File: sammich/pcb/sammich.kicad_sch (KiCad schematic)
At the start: 38 parts, among them J1 Conn_01x02, J2 Conn_02x05_Odd_Even, J3 Conn_01x04, U1 STM32F103RBTx, U2 LD3985M33R_SOT23, U3 MAX485E, Y1 Crystal

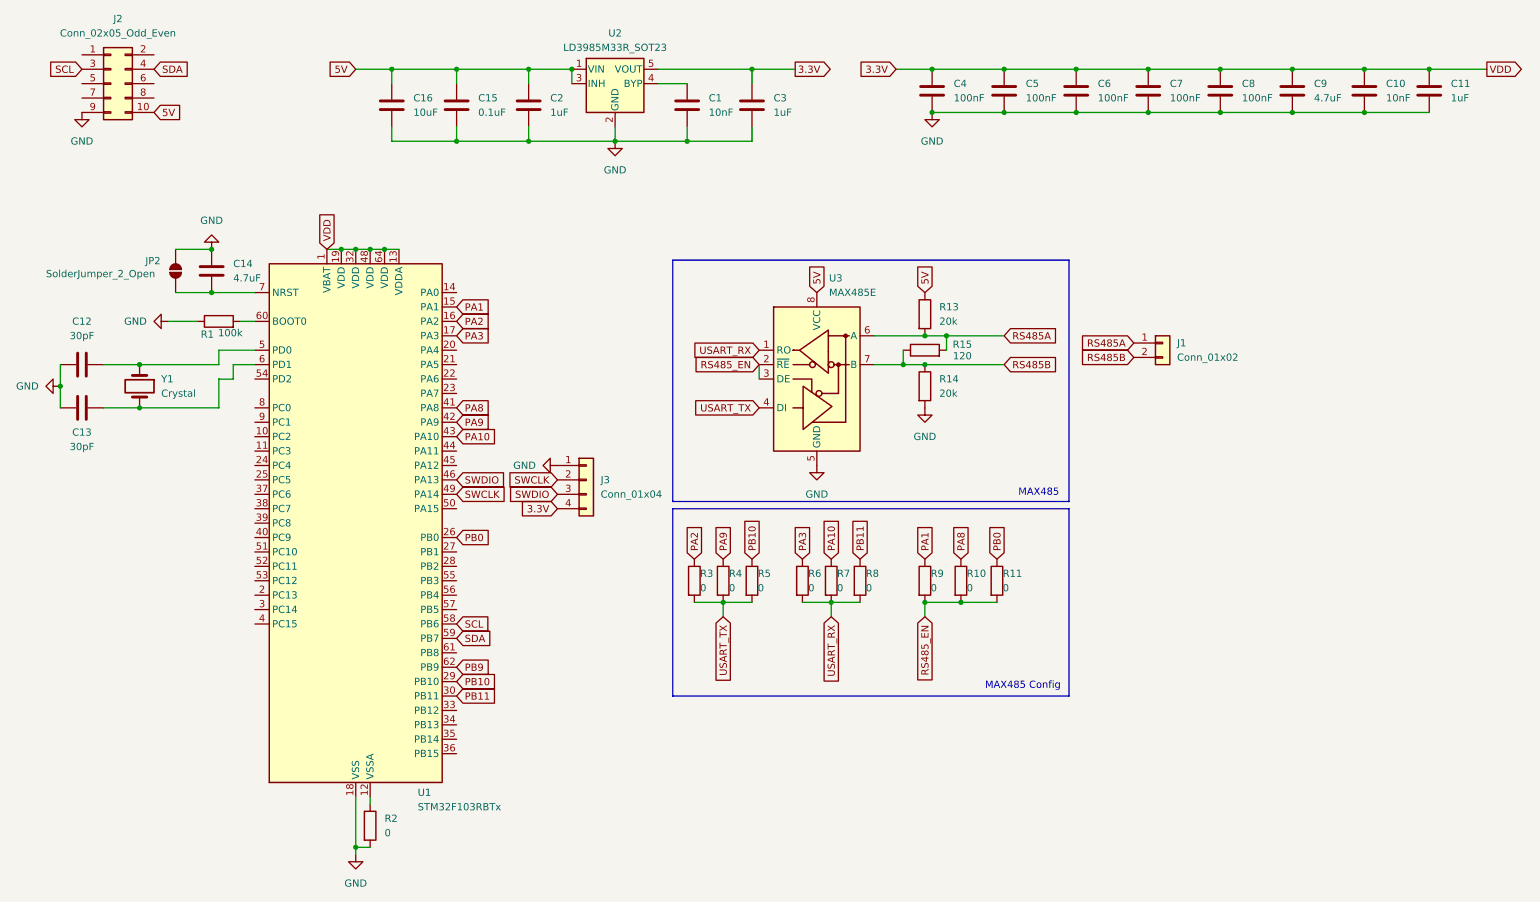
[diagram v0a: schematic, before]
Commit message: Updated PCB to use I2C
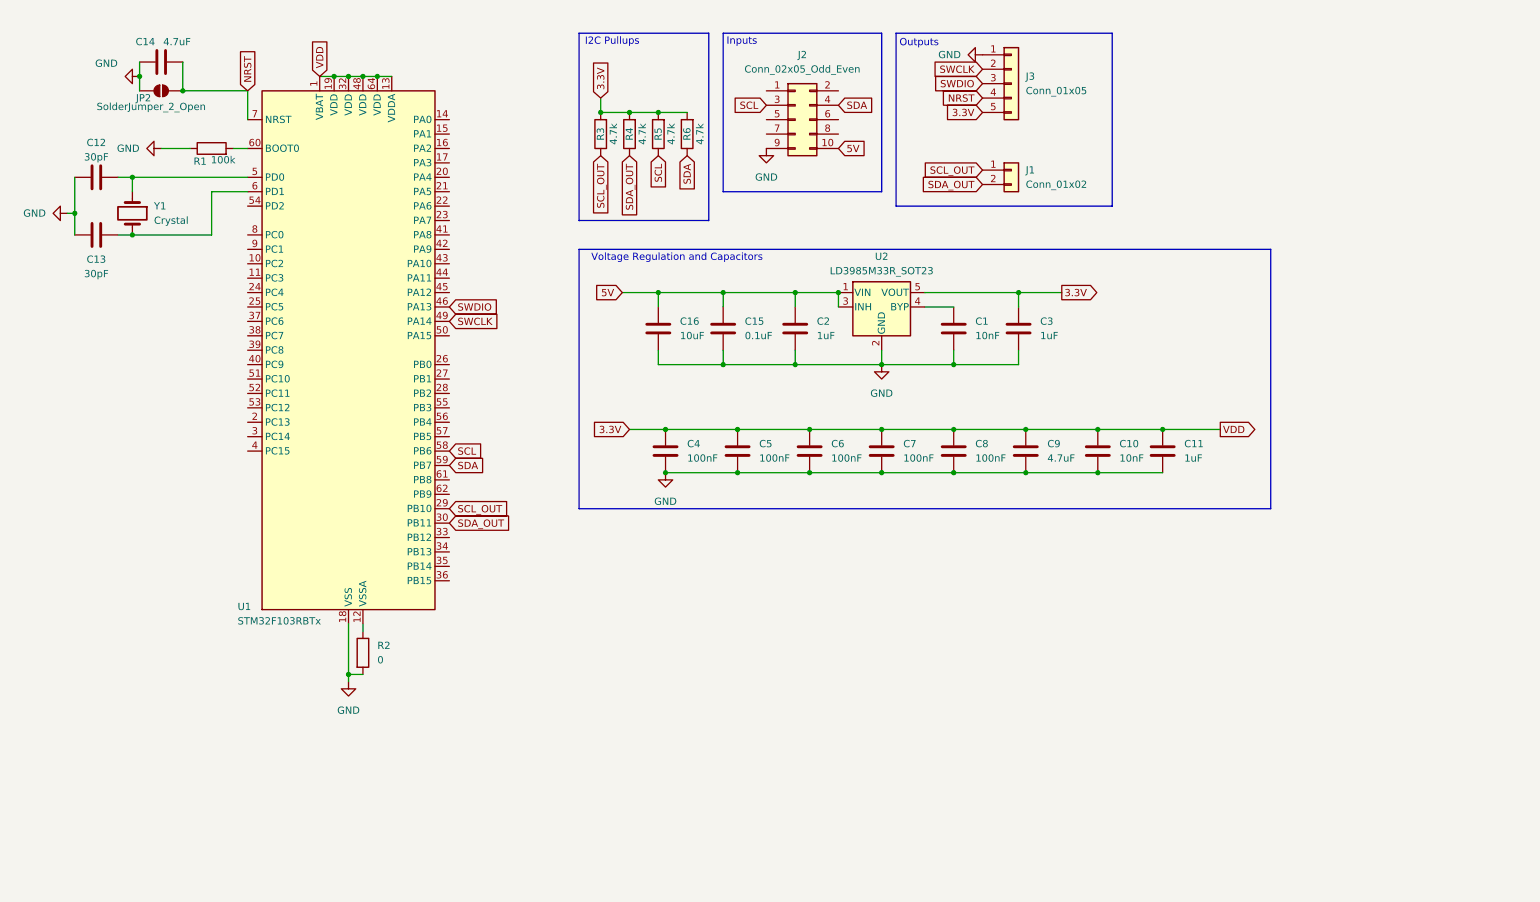
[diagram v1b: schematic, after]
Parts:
- removed J3: Conn_01x04, Connector_PinSocket_2.54mm:PinSocket_1x04_P2.54mm_Vertical, symbol Connector_Generic:Conn_01x04
- removed R10, R11, R7, R8, R9: 0, Resistor_SMD:R_0201_0603Metric, symbol Device:R
- removed R13, R14: 20k, Resistor_SMD:R_0201_0603Metric, symbol Device:R
- removed R15: 120, Resistor_SMD:R_0201_0603Metric, symbol Device:R
- removed U3: MAX485E, Package_SO:SOIC-8_3.9x4.9mm_P1.27mm, symbol Interface_UART:MAX485E
- added J3: Conn_01x05, Connector_PinHeader_2.54mm:PinHeader_1x05_P2.54mm_Vertical, symbol Connector_Generic:Conn_01x05
- J2: footprint Connector_PinHeader_2.54mm:PinHeader_2x05_P2.54mm_Vertical -> Connector_PinSocket_2.54mm:PinSocket_2x05_P2.54mm_Vertical
- R3, R4, R5, R6: value 0 -> 4.7k
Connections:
- net RS485A is gone; now on net SCL_OUT: J1.1 (Pin_1)
- net RS485B is gone; now on net SDA_OUT: J1.2 (Pin_2)
- net USART_RX is gone; now on net 3.3V: R6.2
- net USART_TX is gone; now on net 3.3V: R3.2, R4.2, R5.2
- net 3.3V: now also J3.5 (Pin_5)
- net GND: now also J3.1 (Pin_1)
- net SCL: now also R5.1
- net SDA: now also R6.1
- net SWCLK: now also J3.2 (Pin_2)
- net SWDIO: now also J3.3 (Pin_3)
- net NRST: now reaches C14.2, JP2.2 (B), U1.7 (NRST)
- net NRST: now also J3.4 (Pin_4)
- net PA1: no longer names the net of U1.15 (PA1)
- net PA10: no longer names the net of U1.43 (PA10)
- net PA2: no longer names the net of U1.16 (PA2)
- net PA2: no longer R3.1
- net PA3: no longer names the net of U1.17 (PA3)
- net PA3: no longer R6.1
- net PA8: no longer names the net of U1.41 (PA8)
- net PA9: no longer names the net of U1.42 (PA9)
- net PA9: no longer R4.1
- net PB0: no longer names the net of U1.26 (PB0)
- net PB10 renamed SCL_OUT
- net SCL_OUT: now also R3.1; no longer R5.1
- net PB11 renamed SDA_OUT
- net SDA_OUT: now also R4.1
- net PB9: no longer names the net of U1.62 (PB9)
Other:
- note added: "I2C Pullups"
- note added: "Inputs"
- note added: "Outputs"
- note added: "Voltage Regulation and Capacitors"
- note removed: "MAX485"
- note removed: "MAX485 Config"
- company: (none) -> Oregon State University
- title: (none) -> Interpretation Layer
- moved on the sheet: C1, C10, C11, C12, C13, C14, C15, C16, C2, C3, C4, C5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
